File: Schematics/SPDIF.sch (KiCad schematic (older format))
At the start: 13 parts, among them U501 IC-SPDIF-RX-OPTO, U502 IC-SPDIF-TX-OPTO

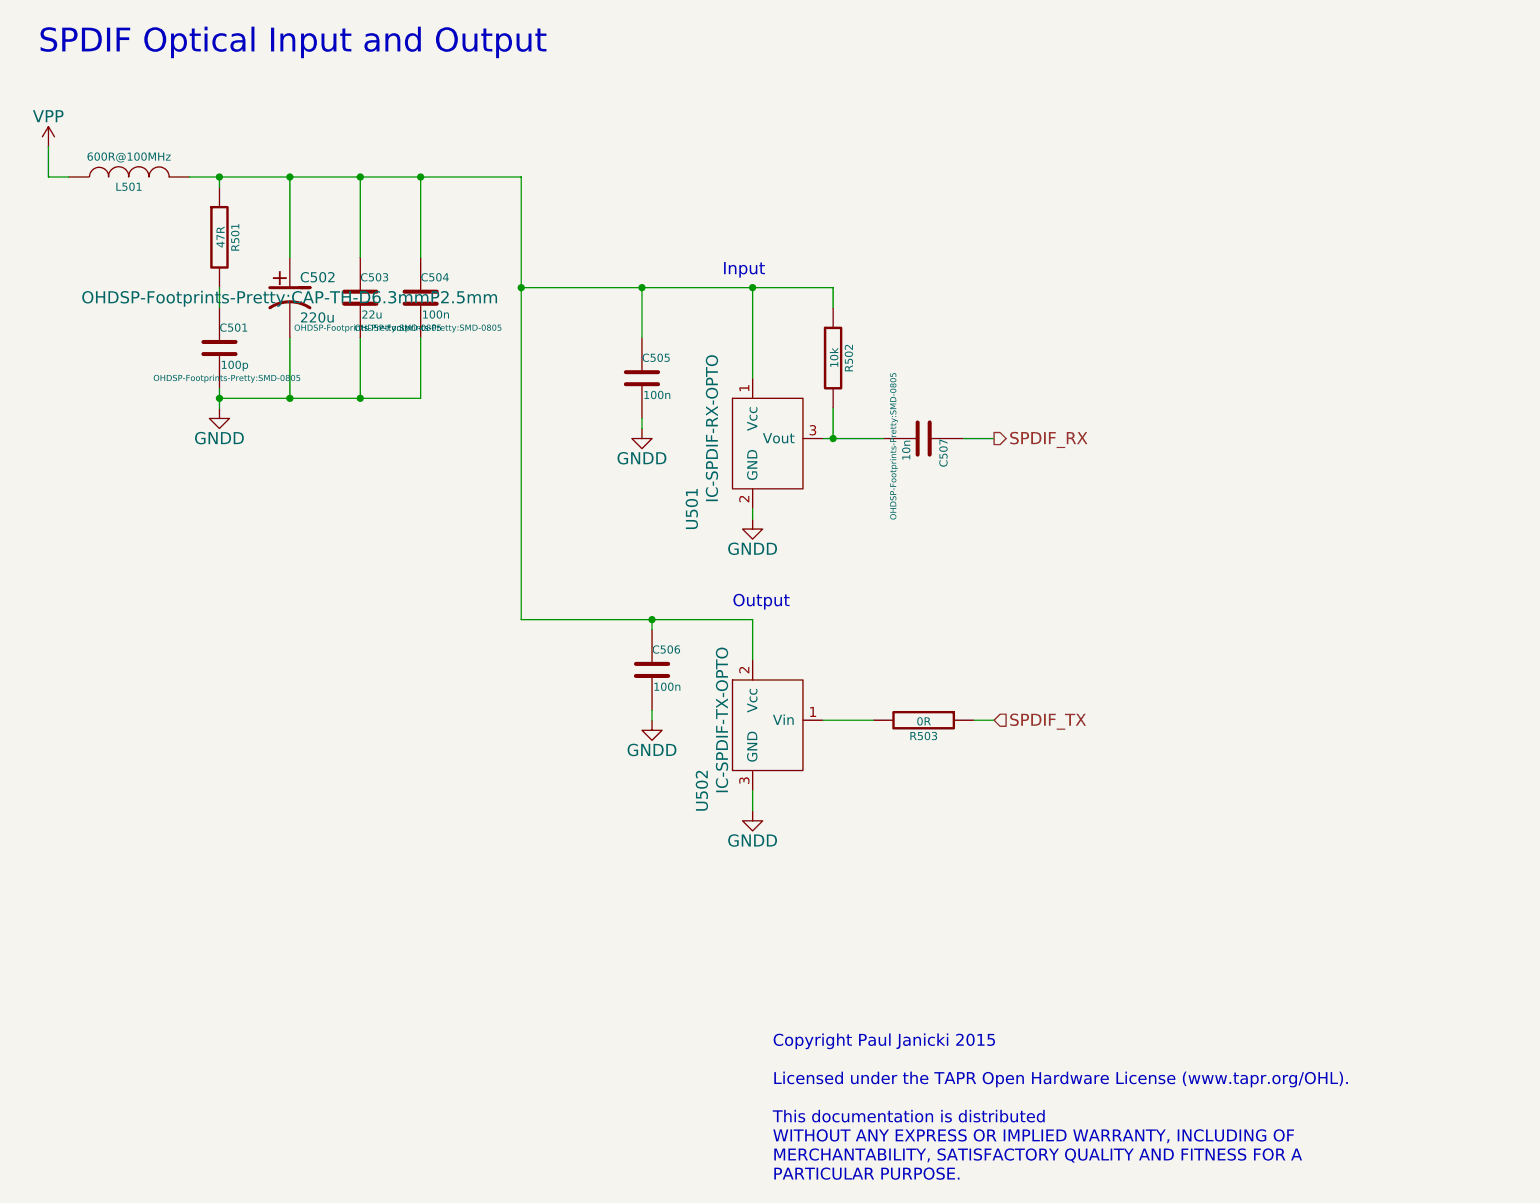
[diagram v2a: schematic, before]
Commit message: PCB work, SPDIF filter caps changed
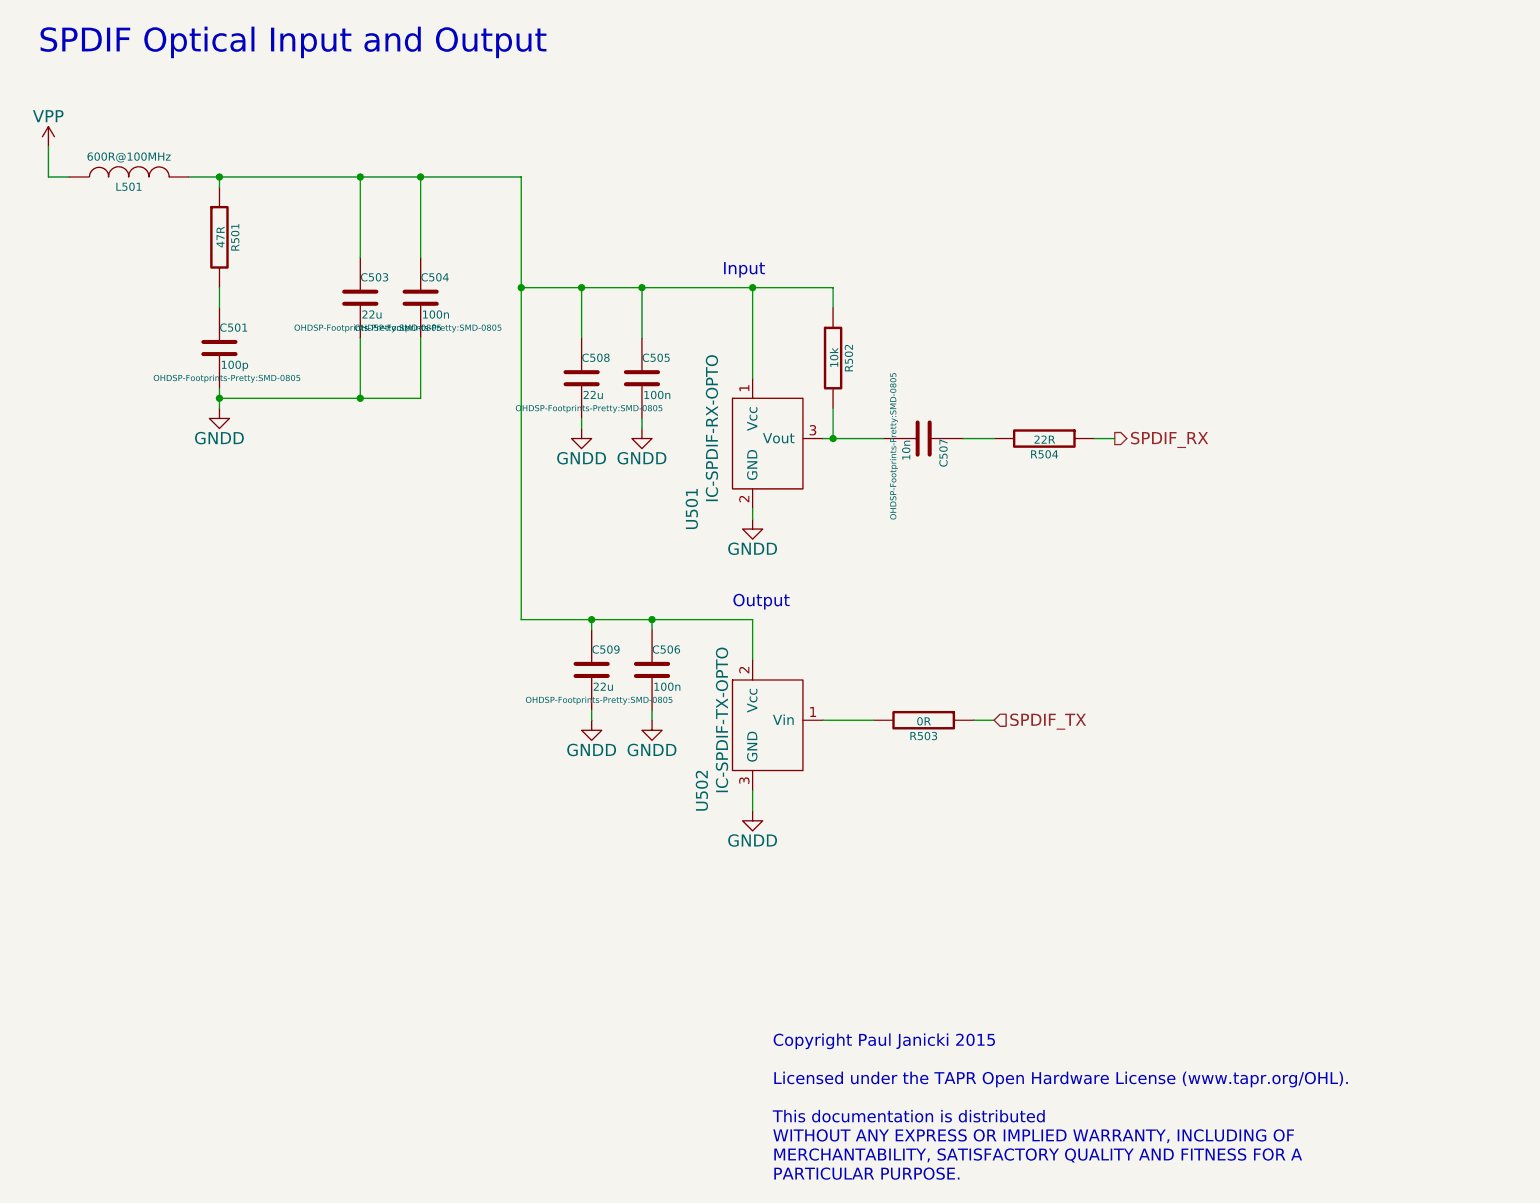
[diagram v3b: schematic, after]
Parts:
- removed C502: 220u, OHDSP-Footprints-Pretty:CAP-TH-D6.3mmP2.5mm, symbol CP1
- added C508, C509: 22u, OHDSP-Footprints-Pretty:SMD-0805, symbol C
- added R504: 22R, OHDSP-Footprints-Pretty:SMD-0805, symbol R
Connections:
- net GNDD: now also C508.2, C509.2
- net SPDIF_RX: now also R504.1; no longer C507.1
- net at C503.1, C504.1, C505.1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: now also C508.1, C509.1
- new net: C507.1, R504.2
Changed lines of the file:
@@
-$EndComp
-$Comp
-L CP1 C502
-U 1 1 54E24758
-P 4600 2700
-F 0 "C502" H 4650 2800 50  0000 L CNN
-F 1 "220u" H 4650 2600 50  0000 L CNN
-F 2 "OHDSP-Footprints-Pretty:CAP-TH-D6.3mmP2.5mm" H 4600 2700 60  0000 C CNN
-F 3 "~" H 4600 2700 60  0000 C CNN
-	1    4600 2700
-	1    0    0    -1
 $EndComp
 $Comp
@@
 Text Notes 6800 4250 0    60   ~ 0
 Output
-Text HLabel 8100 3400 2    60   Output ~ 0
+Text HLabel 8700 3400 2    60   Output ~ 0
 SPDIF_RX
 Text HLabel 8100 4800 2    60   Input ~ 0
@@
 Wire Wire Line
 	4250 2650 4250 2750
-Wire Wire Line
-	4600 2100 4600 2500
 Connection ~ 4250 2100
 Wire Wire Line
 	4950 2100 4950 2500
-Connection ~ 4600 2100
 Connection ~ 4950 2100
 Wire Wire Line
@@
 Wire Wire Line
 	4250 3200 5250 3200
-Wire Wire Line
-	4600 3200 4600 2900
 Connection ~ 4250 3200
 Wire Wire Line
 	4950 3200 4950 2900
-Connection ~ 4600 3200
 Connection ~ 4950 3200
 Wire Wire Line
@@
 Text Notes 7000 7100 0    59   ~ 0
 Copyright Paul Janicki 2015\n\nLicensed under the TAPR Open Hardware License (www.tapr.org/OHL).\n\nThis documentation is distributed\nWITHOUT ANY EXPRESS OR IMPLIED WARRANTY, INCLUDING OF\nMERCHANTABILITY, SATISFACTORY QUALITY AND FITNESS FOR A\nPARTICULAR PURPOSE.\n
+$Comp
+L R R504
+U 1 1 55004FB3
+P 8350 3400
+F 0 "R504" V 8430 3400 40  0000 C CNN
+F 1 "22R" V 8357 3401 40  0000 C CNN
+F 2 "OHDSP-Footprints-Pretty:SMD-0805" V 8280 3400 30  0001 C CNN
+F 3 "~" H 8350 3400 30  0000 C CNN
+	1    8350 3400
+	0    1    1    0
+$EndComp
+Wire Wire Line
+	8700 3400 8600 3400
+$Comp
+L C C508
+U 1 1 5500568E
+P 6050 3100
+F 0 "C508" H 6050 3200 40  0000 L CNN
+F 1 "22u" H 6056 3015 40  0000 L CNN
+F 2 "OHDSP-Footprints-Pretty:SMD-0805" H 6088 2950 30  0000 C CNN
+F 3 "~" H 6050 3100 60  0000 C CNN
+	1    6050 3100
+	1    0    0    -1
+$EndComp
+$Comp
+L C C509
+U 1 1 550056ED
+P 6100 4550
+F 0 "C509" H 6100 4650 40  0000 L CNN
+F 1 "22u" H 6106 4465 40  0000 L CNN
+F 2 "OHDSP-Footprints-Pretty:SMD-0805" H 6138 4400 30  0000 C CNN
+F 3 "~" H 6100 4550 60  0000 C CNN
+	1    6100 4550
+	1    0    0    -1
+$EndComp
+$Comp
+L GNDD #PWR0102
+U 1 1 5500577B
+P 6050 3350
+F 0 "#PWR0102" H 6050 3100 60  0001 C CNN
+F 1 "GNDD" H 6050 3200 60  0000 C CNN
+F 2 "" H 6050 3350 60  0000 C CNN
+F 3 "" H 6050 3350 60  0000 C CNN
+	1    6050 3350
+	1    0    0    -1
+$EndComp
+$Comp
+L GNDD #PWR0103
+U 1 1 55005796
+P 6100 4800
+F 0 "#PWR0103" H 6100 4550 60  0001 C CNN
+F 1 "GNDD" H 6100 4650 60  0000 C CNN
+F 2 "" H 6100 4800 60  0000 C CNN
+F 3 "" H 6100 4800 60  0000 C CNN
+	1    6100 4800
+	1    0    0    -1
+$EndComp
+Wire Wire Line
+	6100 4800 6100 4750
+Wire Wire Line
+	6100 4350 6100 4300
+Connection ~ 6100 4300
+Wire Wire Line
+	6050 3350 6050 3300
+Wire Wire Line
+	6050 2900 6050 2650
+Connection ~ 6050 2650
 $EndSCHEMATC
